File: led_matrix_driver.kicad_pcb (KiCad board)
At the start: 4 copper layers, 100 x 100 mm, 61 parts, among them J2 Screw_Terminal_01x02, J3 Screw_Terminal_01x02, J4 Conn_01x06_Pin, J5 Conn_02x17_Odd_Even, Q1 PXN020-100QSJ, Q2 TPH4R50ANH1,LQ, SW1 CK_KMS2xxGP, SW2 CK_KMS2xxGP, U1 LV5144RGYR, U2 Pico, U3 ESP32-WROOM-32, U4 AP1117-33, U6 Teensy4.0, U7 74AHCT541, U8 74AHCT541

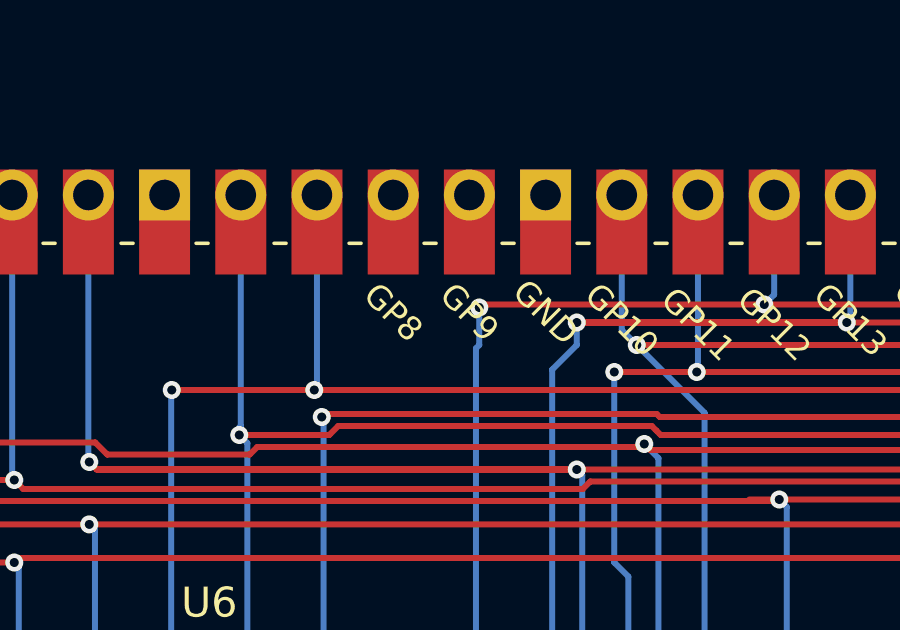
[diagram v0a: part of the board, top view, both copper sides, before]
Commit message: Updated packages. Added OE to RPi Pico
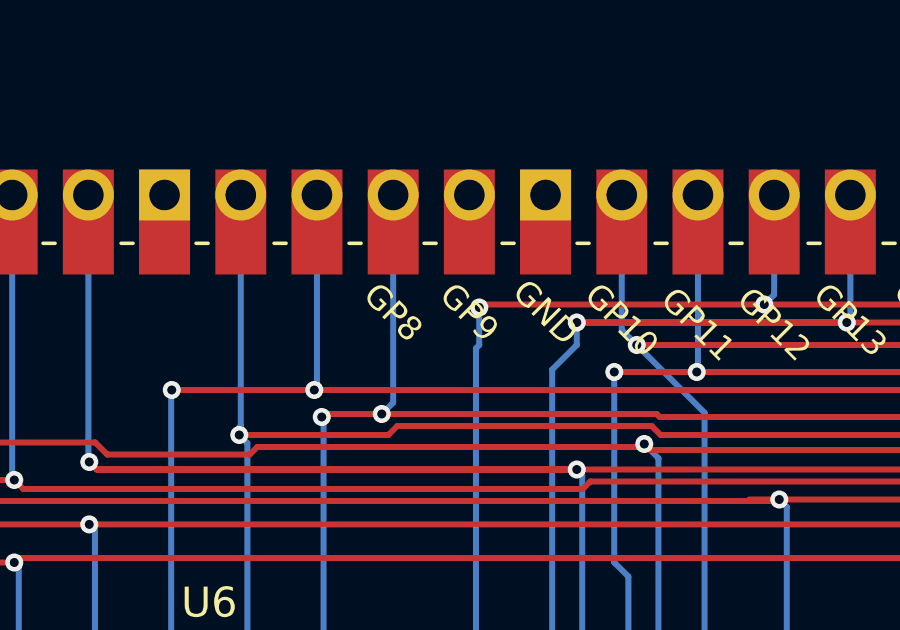
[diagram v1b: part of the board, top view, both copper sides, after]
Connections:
- U2 pad 11: /CTL -> /OE
- U2 pad 12: /DATA -> unconnected-(U2-GPIO9-Pad12)
- U2 pad 33: unconnected-(U2-AGND-Pad33) -> GND
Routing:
- net /OE: track 154.1 -> 161.5 mm, vias 5 -> 6

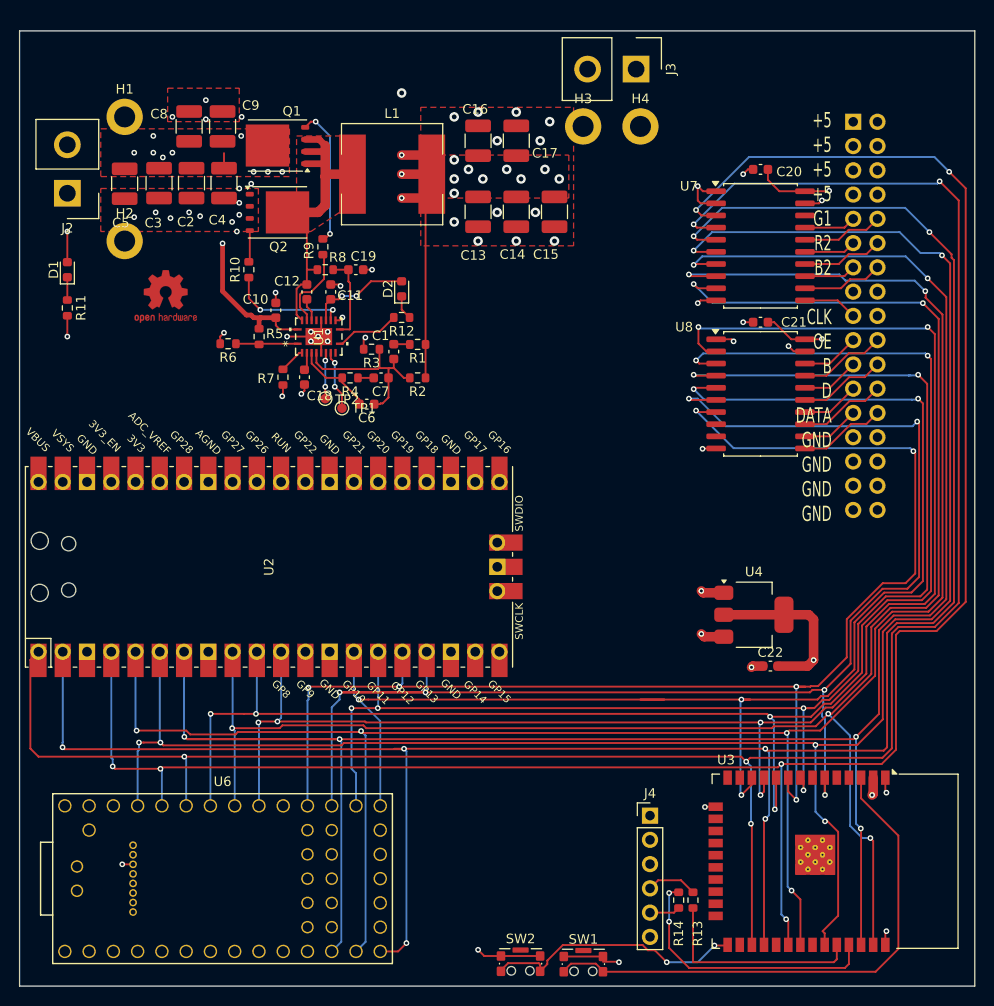
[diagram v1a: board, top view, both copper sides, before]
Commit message: Some mounting holes. Release to prod
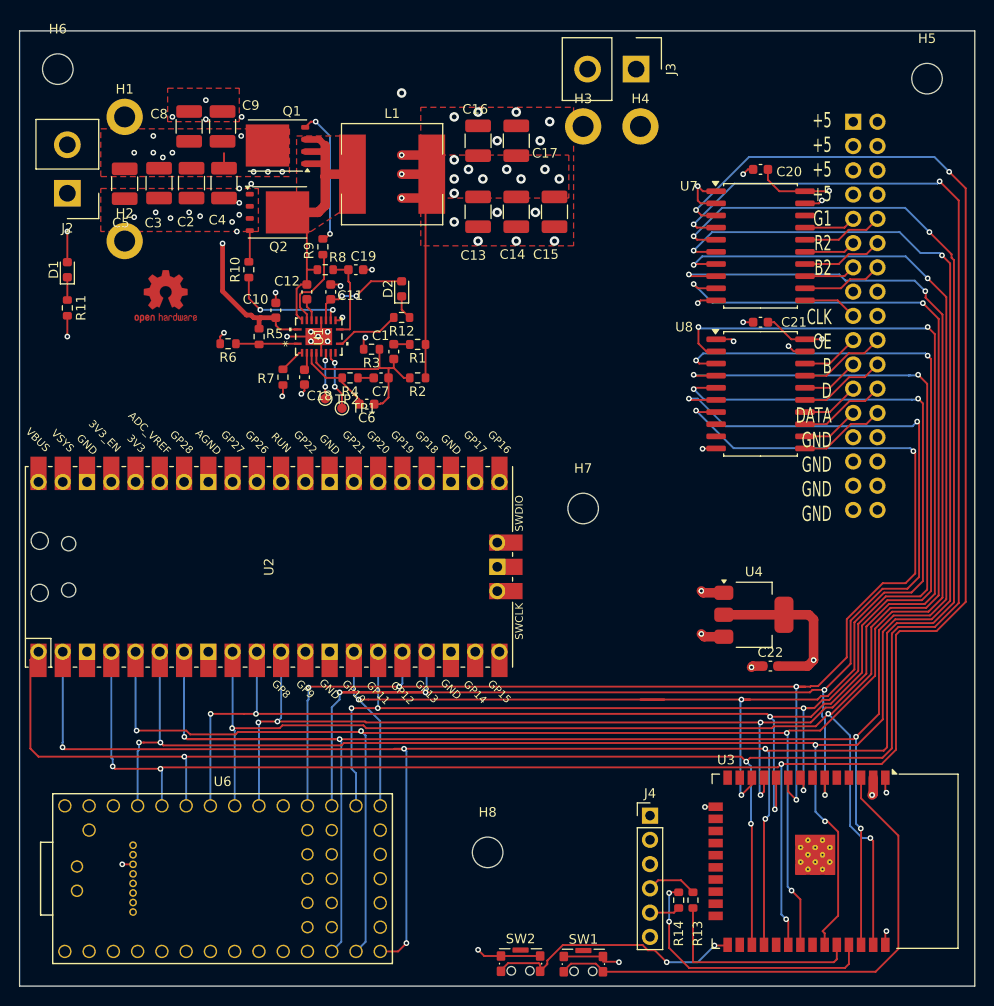
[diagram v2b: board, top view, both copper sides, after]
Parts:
- added H5: MountingHole, MountingHole:MountingHole_3.2mm_M3, F.Cu at (145.0, 55.0)
- added H6: MountingHole, MountingHole:MountingHole_3.2mm_M3, F.Cu at (54.0, 54.0)
- added H7: MountingHole, MountingHole:MountingHole_3.2mm_M3, F.Cu at (109.0, 100.0)
- added H8: MountingHole, MountingHole:MountingHole_3.2mm_M3, F.Cu at (99.0, 136.0)
